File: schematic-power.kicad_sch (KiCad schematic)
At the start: 32 parts, among them U4 TPS62933, U9 TPS62933

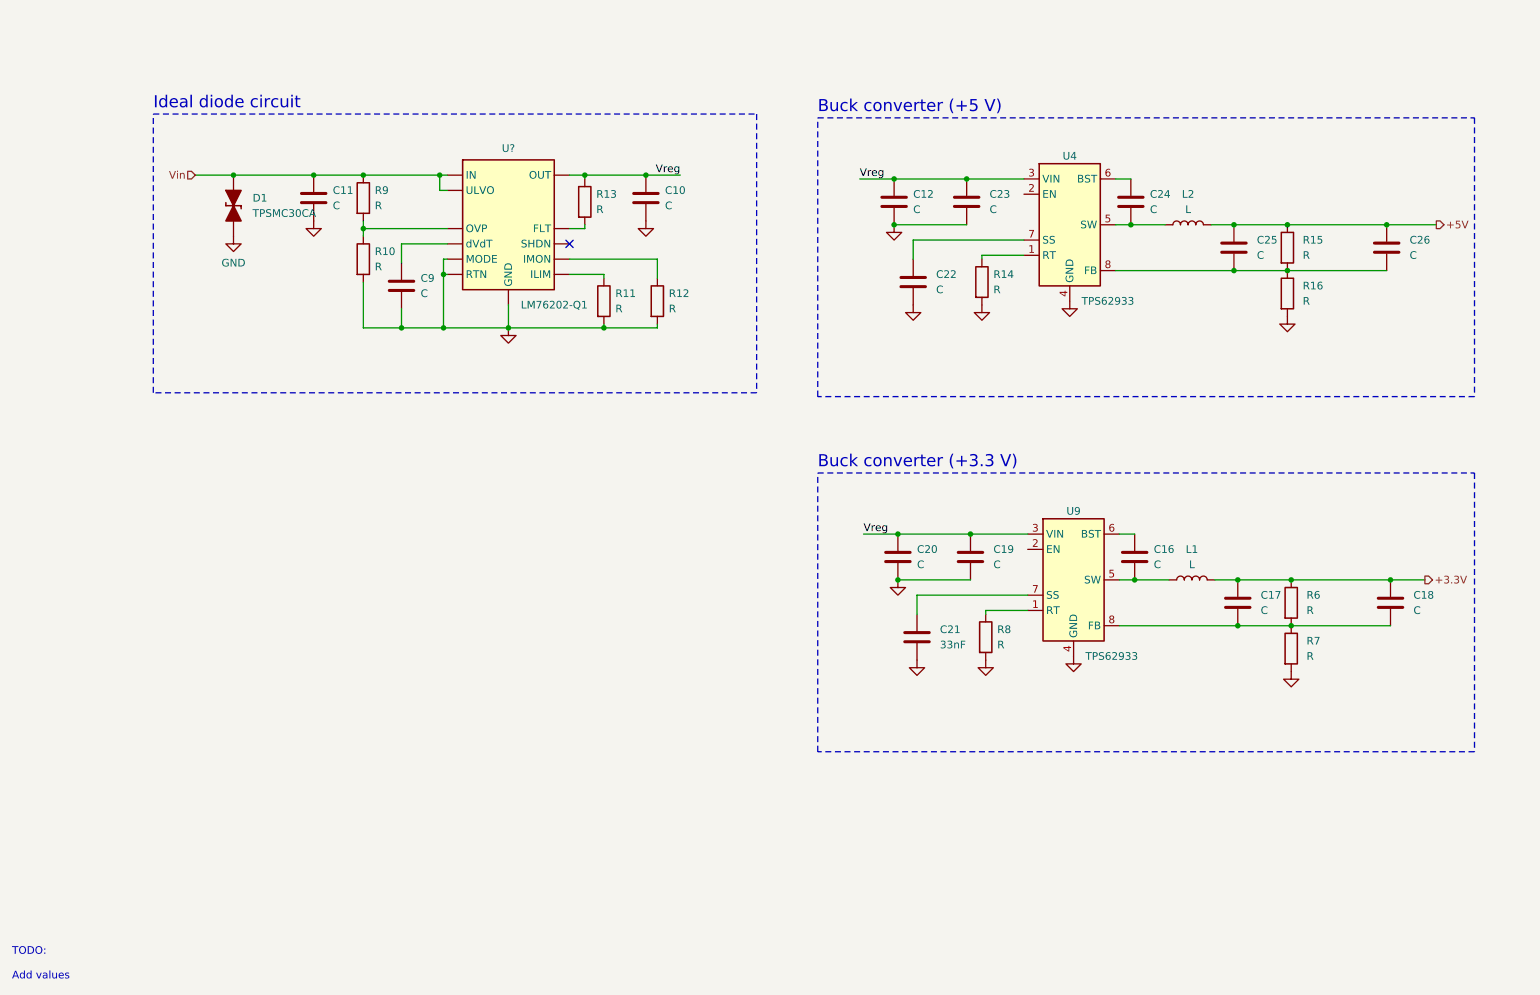
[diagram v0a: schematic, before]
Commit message: Repair & add IO schema
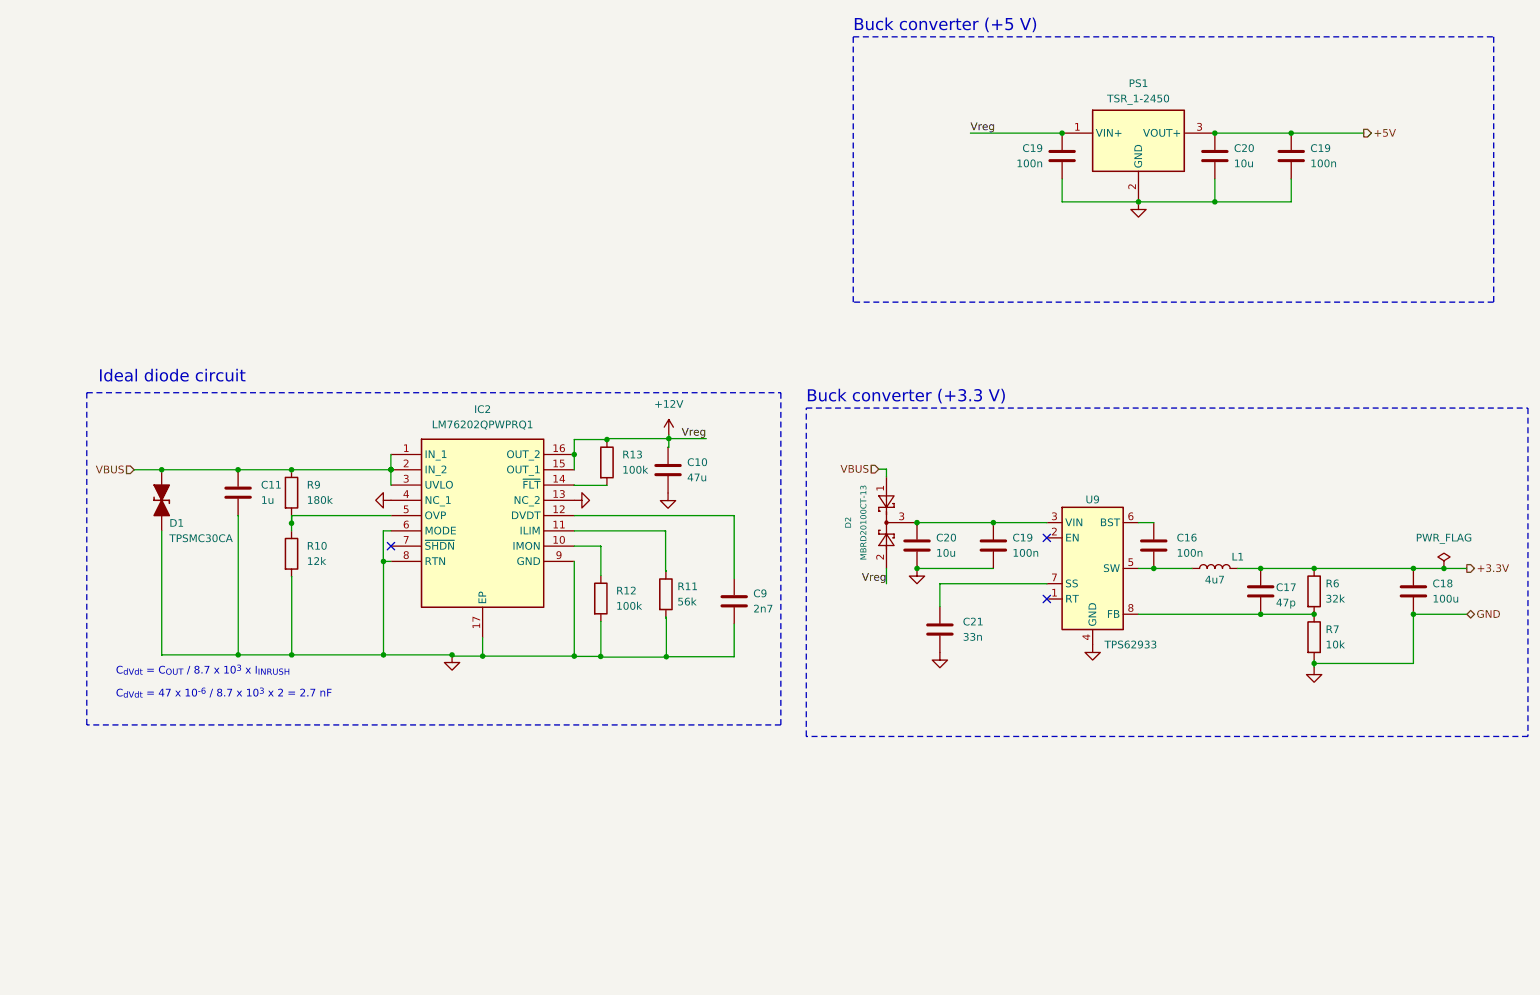
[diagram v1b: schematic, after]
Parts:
- removed C12, C22, C23, C24, C25, C26: C, symbol Device:C
- removed L2: L, symbol Device:L
- removed R14, R15, R16, R8: R, symbol Device:R
- removed U4: TPS62933, Package_TO_SOT_SMD:SOT-583-8, symbol Regulator_Switching:TPS62933
- removed U?: LM76202-Q1, symbol Hydros:LM76202-Q1
- added C19 (x2): 100n, Capacitor_SMD:C_1206_3216Metric, symbol Device:C
- added C20: 10u, Capacitor_SMD:CP_Elec_8x10.5, symbol Device:C
- added D2: MBRD20100CT-13, MBRD20100CT-13:TO252_(DPAK)_1, symbol Diode:BAS40-04
- added IC2: LM76202QPWPRQ1, mbr:SOP65P640X120-17N, symbol Lm7602 ideal diode:LM76202QPWPRQ1
- added PS1: TSR_1-2450, TSR-1-24120, symbol Tracko 1-2450 5V:TSR_1-2450
- C10: value C -> 47u; footprint (none) -> Capacitor_SMD:CP_Elec_6.3x7.7
- C11: value C -> 1u; footprint (none) -> Capacitor_SMD:C_1206_3216Metric
- C16, C19: value C -> 100n; footprint (none) -> Capacitor_SMD:C_1206_3216Metric
- C17: value C -> 47p; footprint (none) -> Capacitor_SMD:C_1206_3216Metric
- C18: value C -> 100u; footprint (none) -> Capacitor_SMD:CP_Elec_8x10.5
- C20: value C -> 10u; footprint (none) -> Capacitor_SMD:CP_Elec_8x10.5
- C21: value 33nF -> 33n; footprint (none) -> Capacitor_SMD:C_1206_3216Metric
- C9: value C -> 2n7; footprint (none) -> Capacitor_SMD:C_1206_3216Metric
- D1: footprint Diode_SMD_AKL:D_SMC_TVS -> lib:TPSMCSeries_LTF
- L1: value L -> 4u7; footprint (none) -> library:SRN3015TA4R7M
- R10: value R -> 12k; footprint (none) -> Resistor_SMD:R_1206_3216Metric
- R11: value R -> 56k; footprint (none) -> Resistor_SMD:R_1206_3216Metric
- R12, R13: value R -> 100k; footprint (none) -> Resistor_SMD:R_1206_3216Metric
- R6: value R -> 32k; footprint (none) -> Resistor_SMD:R_1206_3216Metric
- R7: value R -> 10k; footprint (none) -> Resistor_SMD:R_1206_3216Metric
- R9: value R -> 180k; footprint (none) -> Resistor_SMD:R_1206_3216Metric
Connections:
- net +5V: now also C19.1, C20.1, PS1.3 (VOUT+)
- net GND: now also C18.2, C19.2, C19.2, C20.2, IC2.13 (NC_2), IC2.17 (EP), IC2.4 (NC_1), IC2.6 (MODE), IC2.8 (RTN), IC2.9 (GND), PS1.2 (GND)
- net at C9.1: now also IC2.12 (DVDT)
- net at R13.2: now also IC2.14 (~{FLT})
- net at R12.1: now also IC2.10 (IMON)
- net at R10.1, R9.2: now also IC2.5 (OVP)
- net at R11.1: now also IC2.11 (ILIM)
- net at C17.2, R6.2, R7.1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: no longer C18.2
- net Vin renamed VBUS
- net VBUS: now also D2.1, IC2.1 (IN_1), IC2.2 (IN_2), IC2.3 (UVLO)
- net Vreg: no longer names the net of C19.1, C20.1, U9.3 (VIN)
- net Vreg: now also D2.3; no longer C10.1, R13.1
- new net +12V: C10.1, C19.1, D2.2, IC2.15 (OUT_1), IC2.16 (OUT_2), PS1.1 (VIN+), R13.1
- no-connect marks 1 -> 3
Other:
- note added: "C_{dVdt} = 47 x 10^{-6} / 8.7 x 10^{3} x 2 = 2.7 nF"
- note added: "C_{dVdt} = C_{OUT} / 8.7 x 10^{3} x I_{INRUSH}"
- note removed: "TODO: Add values"
- company: (none) -> Hydrogreen Pollub
- title: (none) -> Fuel Cell Control Unit  (FCCU)
- moved on the sheet: C10, C11, C16, C17, C18, C19, C20, C21, C9, D1, L1, R10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
